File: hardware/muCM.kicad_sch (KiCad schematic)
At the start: 54 parts, among them J1 CDM806-04A-MP-F011-67, J2 USB4105, J3 CDM805-08A-FP-F011-67, Q1 2N7002KL3A-TP, U1 FUSB302B01MPX, U2 TCAN3413DRBR, U3 DRV8955, U5 LMR51610YFDBVR, U6 TPS7B4255DBVR

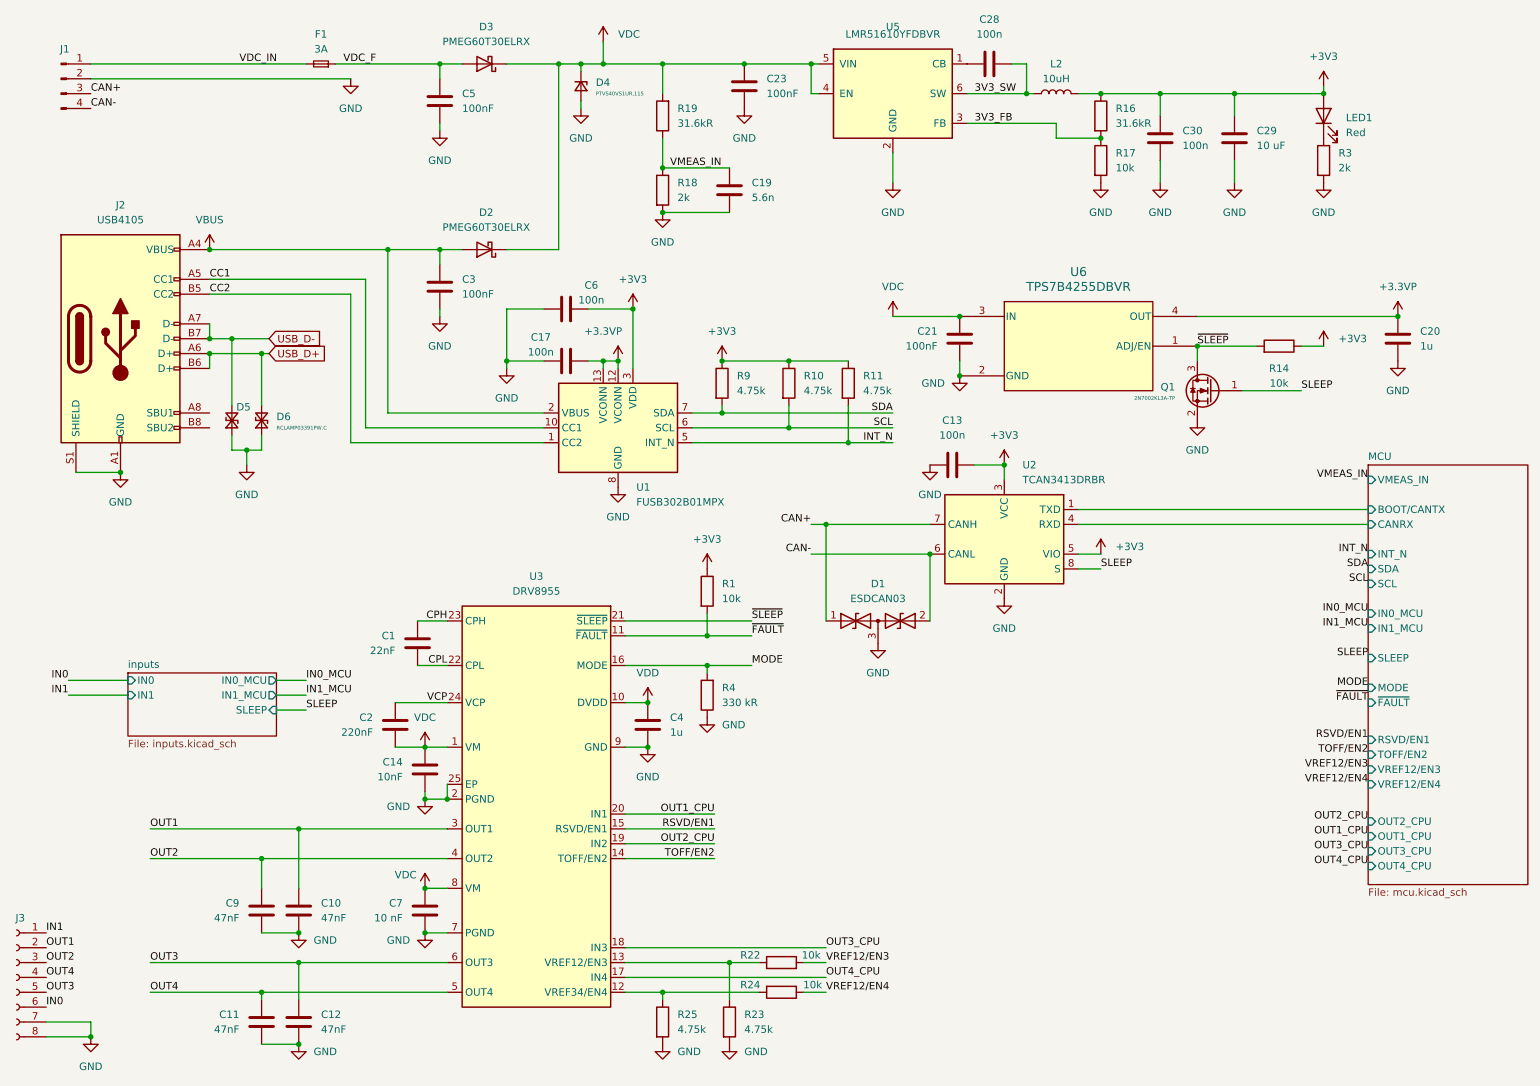
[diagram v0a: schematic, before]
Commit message: finished single board layout - upping to panel size
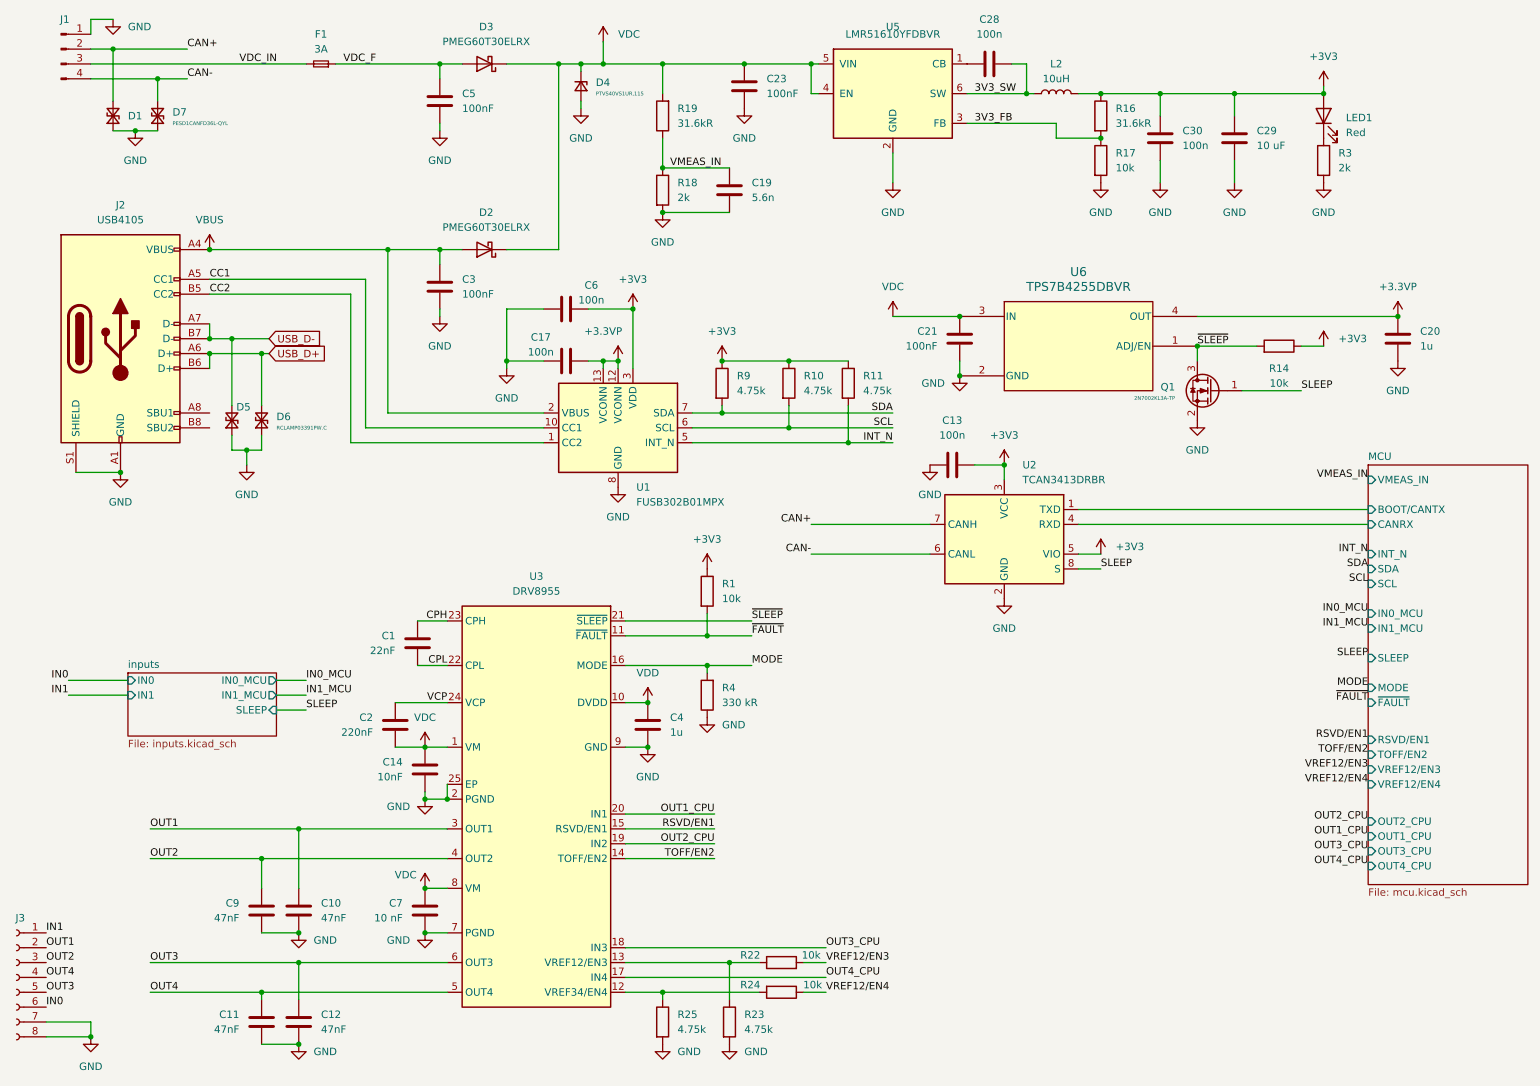
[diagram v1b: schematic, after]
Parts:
- removed D1: ESDCAN03, PCM_PartyWagon112_DFN:DFN1006-3, symbol partywagon112_partdb:ESDCAN03-2BM3Y
- added D1, D7: PESD1CANFD36L-QYL, Diode_SMD:D_SOD-882, symbol partywagon112_partdb:PESD1CANFD36L-QYL
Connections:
- net CAN+: now also J1.2 (Pin_2), D1.2 (A2); no longer J1.3 (Pin_3)
- net CAN-: now also D7.2 (A2)
- net GND: now also J1.1 (Pin_1), D1.1 (A1), D7.1 (A1); no longer J1.2 (Pin_2)
- net VDC_IN: now also J1.3 (Pin_3); no longer J1.1 (Pin_1)
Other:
- moved on the sheet: J1
